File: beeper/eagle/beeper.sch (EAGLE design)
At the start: 32 parts, among them J4 ICSP, T1 MMBT3904, U1 ATA6631, U2 ATMEGA328P, X1 16MHz

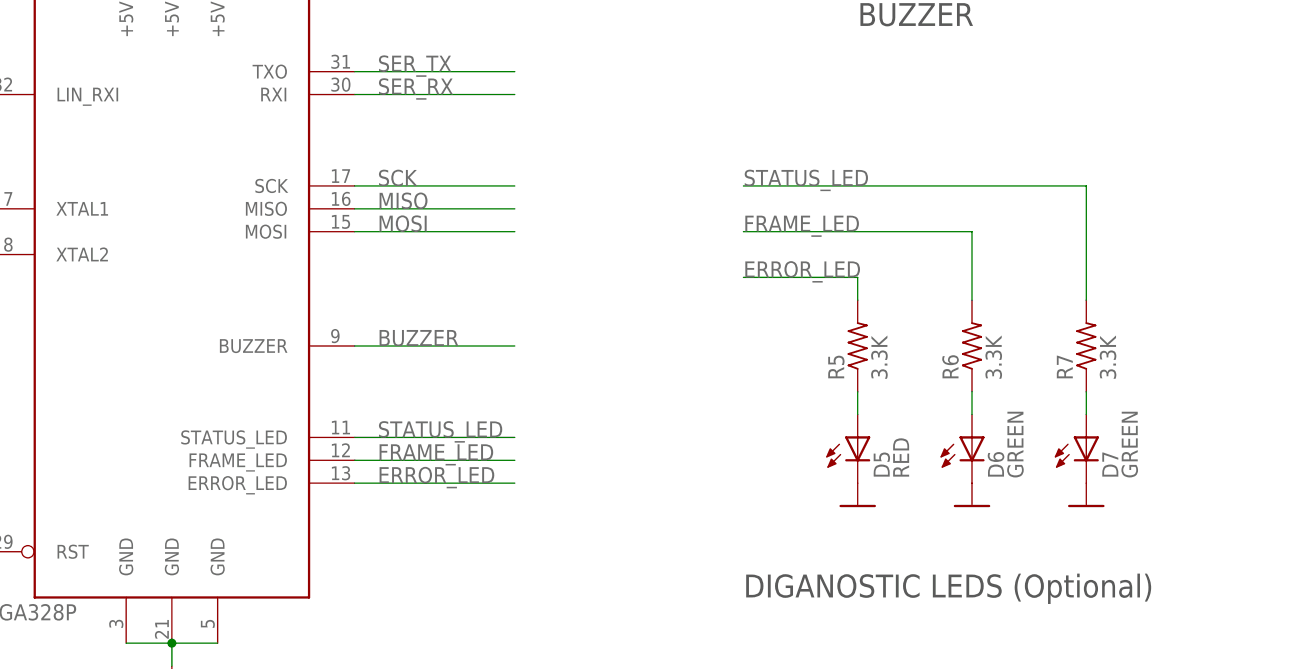
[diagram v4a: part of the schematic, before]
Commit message: Removed the third (status) led.
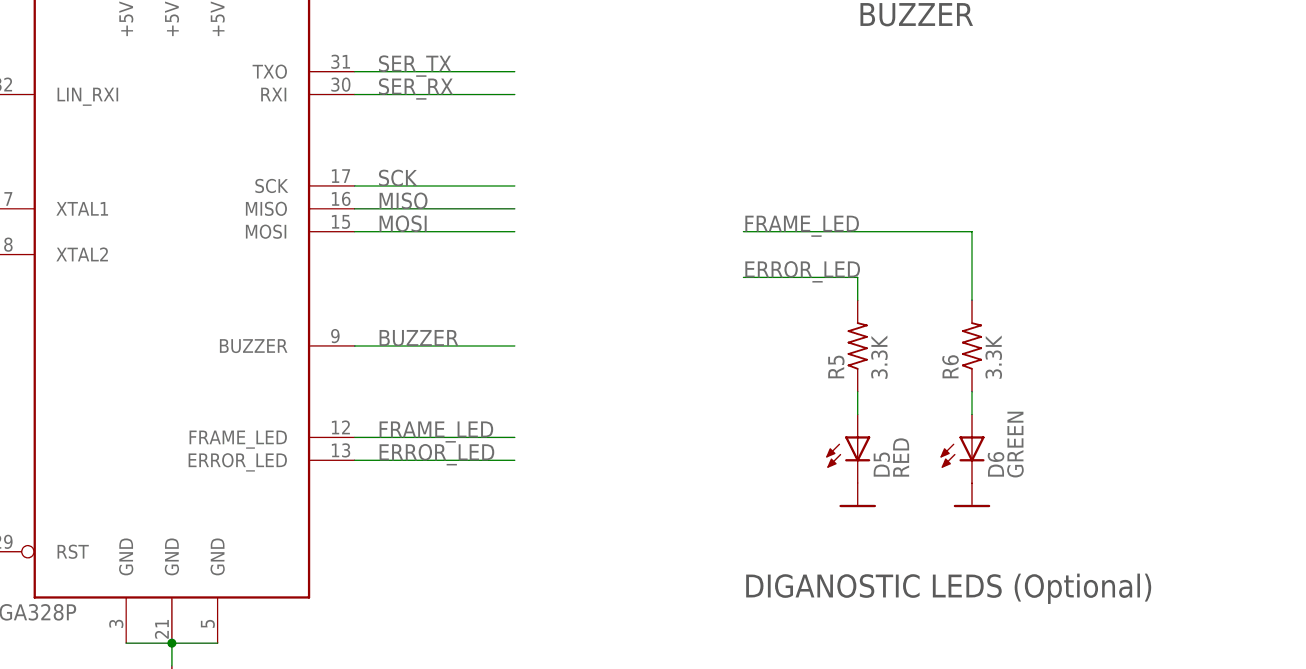
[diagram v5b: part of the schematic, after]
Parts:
- removed D7: GREEN, led:LEDSMT1206
- removed R7: 3.3K, rcl:R-US_R0805
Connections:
- removed net N$2: D7.A, R7.1
- removed net STATUS_LED: R7.2, U2.STATUS_LED
- net GND: no longer D7.C
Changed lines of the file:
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@@
 <part name="R5" library="rcl" deviceset="R-US_" device="R0805" value="3.3K"/>
 <part name="R6" library="rcl" deviceset="R-US_" device="R0805" value="3.3K"/>
-<part name="R7" library="rcl" deviceset="R-US_" device="R0805" value="3.3K"/>
 <part name="C6" library="rcl" deviceset="C-US" device="C0805" value="220pF"/>
 <part name="J1" library="pinhead" deviceset="PINHD-1X3" device=""/>
@@
 <part name="R2" library="rcl" deviceset="R-US_" device="R0805" value="10k"/>
 <part name="GND2" library="beeper" deviceset="GND" device=""/>
-<part name="GND13" library="beeper" deviceset="GND" device=""/>
 <part name="GND16" library="beeper" deviceset="GND" device=""/>
 <part name="J4" library="pinhead" deviceset="PINHD-2X3" device="" value="ICSP"/>
@@
 <part name="D5" library="led" deviceset="LED" device="SMT1206" value="RED"/>
 <part name="D6" library="led" deviceset="LED" device="SMT1206" value="GREEN"/>
-<part name="D7" library="led" deviceset="LED" device="SMT1206" value="GREEN"/>
 <part name="C1" library="rcl" deviceset="CPOL-US" device="UD-6,3X5,8" value="22uF 40V"/>
 <part name="C2" library="rcl" deviceset="C-US" device="C0805" value="0.1uF"/>
@@
 <instance part="R5" gate="G$1" x="261.62" y="99.06" rot="R90"/>
 <instance part="R6" gate="G$1" x="274.32" y="99.06" rot="R90"/>
-<instance part="R7" gate="G$1" x="287.02" y="99.06" rot="R90"/>
 <instance part="C6" gate="G$1" x="99.06" y="154.94"/>
 <instance part="J1" gate="A" x="76.2" y="198.12" rot="MR0"/>
@@
 </instance>
 <instance part="GND2" gate="1" x="274.32" y="81.28"/>
-<instance part="GND13" gate="1" x="287.02" y="81.28"/>
 <instance part="GND16" gate="1" x="185.42" y="60.96"/>
 <instance part="J4" gate="A" x="93.98" y="121.92"/>
@@
 <instance part="D5" gate="G$1" x="261.62" y="88.9"/>
 <instance part="D6" gate="G$1" x="274.32" y="88.9"/>
-<instance part="D7" gate="G$1" x="287.02" y="88.9"/>
 <instance part="C1" gate="G$1" x="152.4" y="195.58" smashed="yes">
 <attribute name="NAME" x="153.416" y="196.215" size="1.778" layer="95"/>
@@
 </segment>
 <segment>
-<pinref part="GND13" gate="1" pin="GND"/>
-<pinref part="D7" gate="G$1" pin="C"/>
-</segment>
-<segment>
 <pinref part="C4" gate="G$1" pin="2"/>
 <pinref part="GND9" gate="1" pin="GND"/>
@@
 <pinref part="C5" gate="G$1" pin="-"/>
 <pinref part="GND10" gate="1" pin="GND"/>
-</segment>
-</net>
-<net name="N$2" class="0">
-<segment>
-<pinref part="R7" gate="G$1" pin="1"/>
-<pinref part="D7" gate="G$1" pin="A"/>
-<wire x1="287.02" y1="93.98" x2="287.02" y2="91.44" width="0.1524" layer="91"/>
 </segment>
 </net>
@@
 </segment>
 <segment>
-<wire x1="205.74" y1="83.82" x2="223.52" y2="83.82" width="0.1524" layer="91"/>
+<wire x1="205.74" y1="86.36" x2="223.52" y2="86.36" width="0.1524" layer="91"/>
 <pinref part="U2" gate="G$1" pin="ERROR_LED"/>
-<label x="208.28" y="83.82" size="1.778" layer="95"/>
+<label x="208.28" y="86.36" size="1.778" layer="95"/>
 </segment>
 </net>
 <net name="FRAME_LED" class="0">
 <segment>
-<wire x1="205.74" y1="86.36" x2="223.52" y2="86.36" width="0.1524" layer="91"/>
+<wire x1="205.74" y1="88.9" x2="223.52" y2="88.9" width="0.1524" layer="91"/>
 <pinref part="U2" gate="G$1" pin="FRAME_LED"/>
-<label x="208.28" y="86.36" size="1.778" layer="95"/>
+<label x="208.28" y="88.9" size="1.778" layer="95"/>
 </segment>
 <segment>
@@
 </segment>
 </net>
-<net name="STATUS_LED" class="0">
-<segment>
-<wire x1="205.74" y1="88.9" x2="223.52" y2="88.9" width="0.1524" layer="91"/>
-<pinref part="U2" gate="G$1" pin="STATUS_LED"/>
-<label x="208.28" y="88.9" size="1.778" layer="95"/>
-</segment>
-<segment>
-<pinref part="R7" gate="G$1" pin="2"/>
-<wire x1="287.02" y1="116.84" x2="287.02" y2="104.14" width="0.1524" layer="91"/>
-<wire x1="248.92" y1="116.84" x2="287.02" y2="116.84" width="0.1524" layer="91"/>
-<label x="248.92" y="116.84" size="1.778" layer="95"/>
-</segment>
-</net>

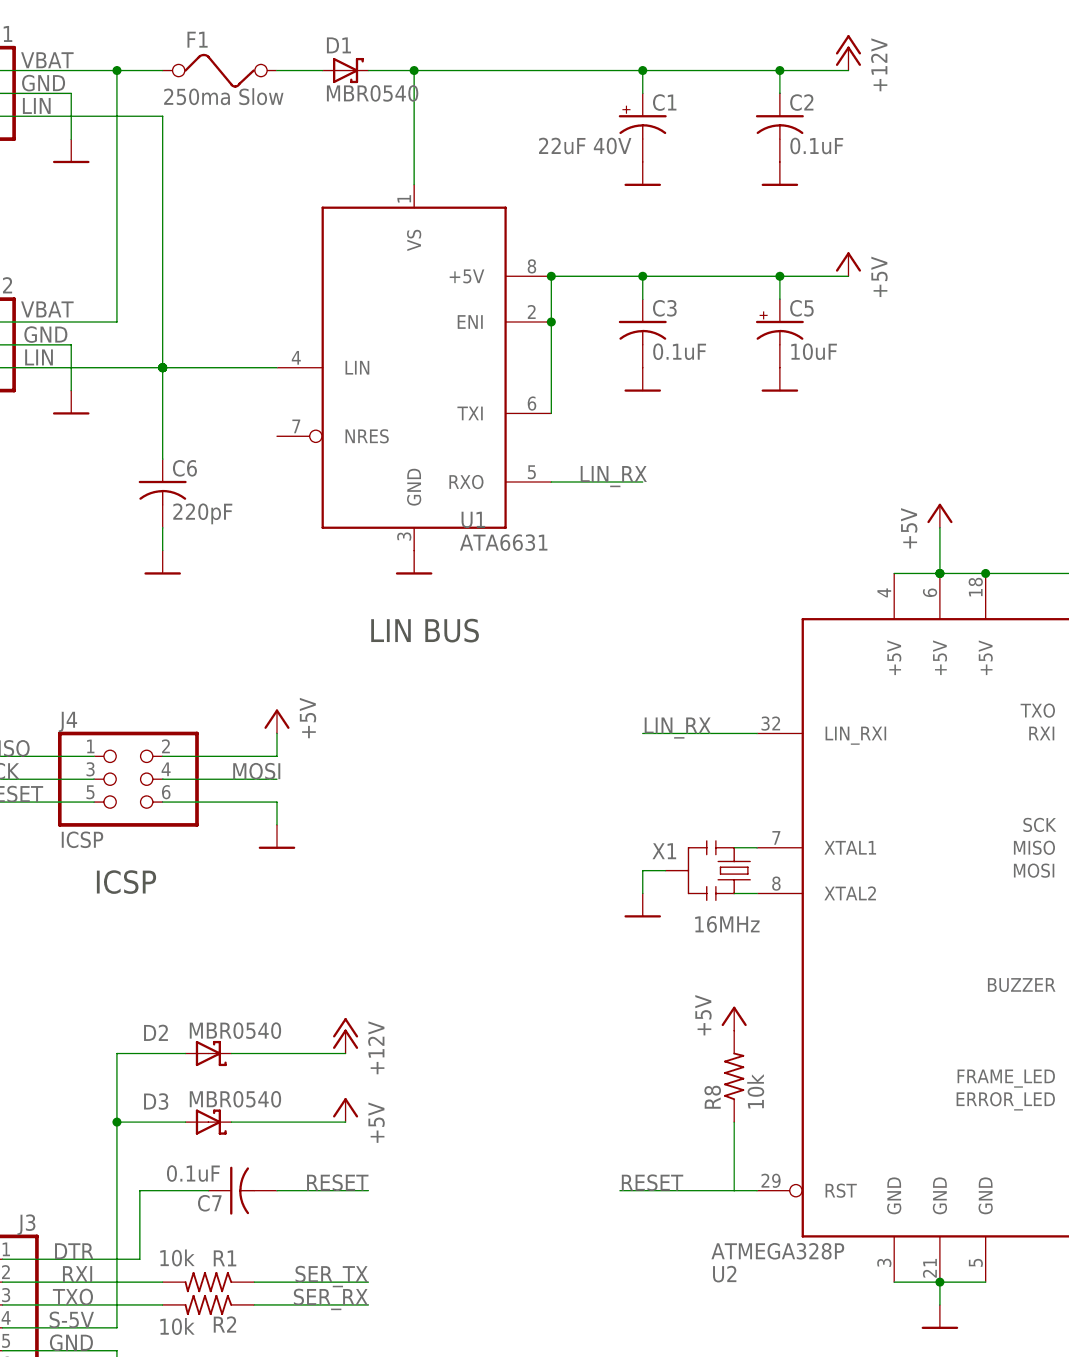
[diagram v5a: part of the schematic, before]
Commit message: Created a clean beeper library. Moved majority of the componnents to the new library.
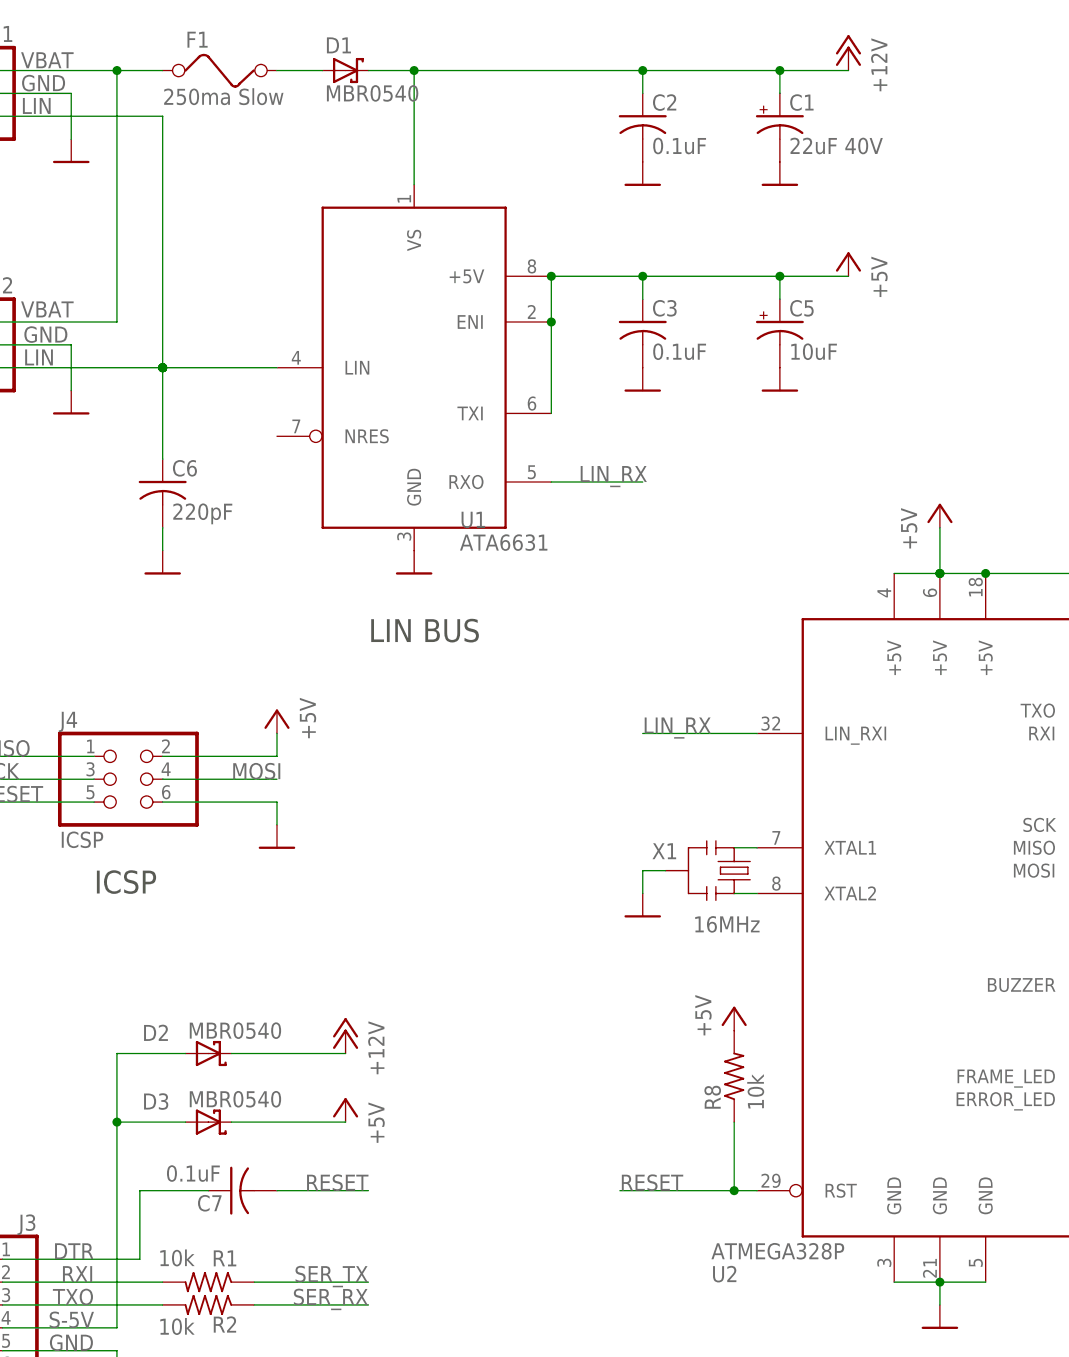
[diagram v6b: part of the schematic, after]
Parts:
- C1: device rcl:CPOL-USUD-6,3X5,8 -> beeper:CPOL-USUD-6,3X5,8
- C2, C3, C6, C7: device rcl:C-USC0805 -> beeper:C-USC0805
- C5: device rcl:CPOL-USA/3216-18R -> beeper:CPOL-USA/3216-18R
- D1, D2, D3, D4: device diode:SMF5.0AT1 -> beeper:SMF5.0AT1
- D5, D6: device led:LEDSMT1206 -> beeper:LEDSMT1206
- J1, J2: device pinhead:PINHD-1X3 -> beeper:PINHD-1X3
- J3: device pinhead:PINHD-1X6 -> beeper:PINHD-1X6
- J4: device pinhead:PINHD-2X3 -> beeper:PINHD-2X3
- R1, R2, R4, R5, R6, R8: device rcl:R-US_R0805 -> beeper:R-US_R0805
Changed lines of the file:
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@@
 </classes>
 <parts>
-<part name="R5" library="rcl" deviceset="R-US_" device="R0805" value="3.3K"/>
-<part name="R6" library="rcl" deviceset="R-US_" device="R0805" value="3.3K"/>
-<part name="C6" library="rcl" deviceset="C-US" device="C0805" value="220pF"/>
-<part name="J1" library="pinhead" deviceset="PINHD-1X3" device=""/>
+<part name="R5" library="beeper" deviceset="R-US_" device="R0805" value="3.3K"/>
+<part name="R6" library="beeper" deviceset="R-US_" device="R0805" value="3.3K"/>
+<part name="C6" library="beeper" deviceset="C-US" device="C0805" value="220pF"/>
+<part name="J1" library="beeper" deviceset="PINHD-1X3" device=""/>
 <part name="FRAME2" library="frames" deviceset="LETTER_L" device=""/>
 <part name="GND3" library="beeper" deviceset="GND" device=""/>
@@
 <part name="GND6" library="beeper" deviceset="GND" device=""/>
 <part name="GND7" library="beeper" deviceset="GND" device=""/>
-<part name="C3" library="rcl" deviceset="C-US" device="C0805" value="0.1uF"/>
+<part name="C3" library="beeper" deviceset="C-US" device="C0805" value="0.1uF"/>
 <part name="GND12" library="beeper" deviceset="GND" device=""/>
-<part name="C7" library="rcl" deviceset="C-US" device="C0805" value="0.1uF"/>
-<part name="P+2" library="supply1" deviceset="+5V" device=""/>
-<part name="R1" library="rcl" deviceset="R-US_" device="R0805" value="10k"/>
-<part name="R2" library="rcl" deviceset="R-US_" device="R0805" value="10k"/>
+<part name="C7" library="beeper" deviceset="C-US" device="C0805" value="0.1uF"/>
+<part name="P+2" library="beeper" deviceset="+5V" device=""/>
+<part name="R1" library="beeper" deviceset="R-US_" device="R0805" value="10k"/>
+<part name="R2" library="beeper" deviceset="R-US_" device="R0805" value="10k"/>
 <part name="GND2" library="beeper" deviceset="GND" device=""/>
 <part name="GND16" library="beeper" deviceset="GND" device=""/>
-<part name="J4" library="pinhead" deviceset="PINHD-2X3" device="" value="ICSP"/>
+<part name="J4" library="beeper" deviceset="PINHD-2X3" device="" value="ICSP"/>
 <part name="GND14" library="beeper" deviceset="GND" device=""/>
-<part name="P+5" library="supply1" deviceset="+5V" device=""/>
+<part name="P+5" library="beeper" deviceset="+5V" device=""/>
 <part name="R3" library="rcl" deviceset="R-US_" device="R0805" value="3.3K"/>
 <part name="T1" library="transistor" deviceset="*-NPN-" device="SOT23-BEC" technology="MMBT3904LT1" value="MMBT3904"/>
 <part name="GND18" library="beeper" deviceset="GND" device=""/>
-<part name="P+3" library="supply1" deviceset="+5V" device=""/>
-<part name="R4" library="rcl" deviceset="R-US_" device="R0805" value="0"/>
-<part name="R8" library="rcl" deviceset="R-US_" device="R0805" value="10k"/>
-<part name="P+6" library="supply1" deviceset="+5V" device=""/>
+<part name="P+3" library="beeper" deviceset="+5V" device=""/>
+<part name="R4" library="beeper" deviceset="R-US_" device="R0805" value="0"/>
+<part name="R8" library="beeper" deviceset="R-US_" device="R0805" value="10k"/>
+<part name="P+6" library="beeper" deviceset="+5V" device=""/>
 <part name="U1" library="beeper" deviceset="ATA6631" device=""/>
-<part name="J3" library="pinhead" deviceset="PINHD-1X6" device=""/>
-<part name="J2" library="pinhead" deviceset="PINHD-1X3" device=""/>
+<part name="J3" library="beeper" deviceset="PINHD-1X6" device=""/>
+<part name="J2" library="beeper" deviceset="PINHD-1X3" device=""/>
 <part name="GND1" library="beeper" deviceset="GND" device=""/>
-<part name="D1" library="diode" deviceset="SMF5.0AT1" device="" value="MBR0540"/>
+<part name="D1" library="beeper" deviceset="SMF5.0AT1" device="" value="MBR0540"/>
 <part name="U2" library="beeper" deviceset="ATMEGA328P" device=""/>
-<part name="D2" library="diode" deviceset="SMF5.0AT1" device="" value="MBR0540"/>
-<part name="D3" library="diode" deviceset="SMF5.0AT1" device="" value="MBR0540"/>
+<part name="D2" library="beeper" deviceset="SMF5.0AT1" device="" value="MBR0540"/>
+<part name="D3" library="beeper" deviceset="SMF5.0AT1" device="" value="MBR0540"/>
 <part name="X1" library="beeper" deviceset="RESONATOR" device="SMD" value="16MHz"/>
 <part name="GND8" library="beeper" deviceset="GND" device=""/>
 <part name="SP1" library="beeper" deviceset="AL60P" device="" value="WT-1205"/>
-<part name="D4" library="diode" deviceset="SMF5.0AT1" device="" value="MBR0540"/>
-<part name="D5" library="led" deviceset="LED" device="SMT1206" value="RED"/>
-<part name="D6" library="led" deviceset="LED" device="SMT1206" value="GREEN"/>
-<part name="C1" library="rcl" deviceset="CPOL-US" device="UD-6,3X5,8" value="22uF 40V"/>
-<part name="C2" library="rcl" deviceset="C-US" device="C0805" value="0.1uF"/>
-<part name="C5" library="rcl" deviceset="CPOL-US" device="A/3216-18R" value="10uF"/>
+<part name="D4" library="beeper" deviceset="SMF5.0AT1" device="" value="MBR0540"/>
+<part name="D5" library="beeper" deviceset="LED" device="SMT1206" value="RED"/>
+<part name="D6" library="beeper" deviceset="LED" device="SMT1206" value="GREEN"/>
+<part name="C1" library="beeper" deviceset="CPOL-US" device="UD-6,3X5,8" value="22uF 40V"/>
+<part name="C2" library="beeper" deviceset="C-US" device="C0805" value="0.1uF"/>
+<part name="C5" library="beeper" deviceset="CPOL-US" device="A/3216-18R" value="10uF"/>
 <part name="C4" library="rcl" deviceset="C-US" device="C0805" value="0.1uF"/>
 <part name="GND9" library="beeper" deviceset="GND" device=""/>
@@
 <part name="GND11" library="beeper" deviceset="GND" device=""/>
 <part name="F1" library="beeper" deviceset="FUSE" device="" value="250ma Slow"/>
-<part name="P+4" library="supply1" deviceset="+5V" device=""/>
-<part name="P+7" library="supply1" deviceset="+12V" device=""/>
-<part name="P+8" library="supply1" deviceset="+5V" device=""/>
-<part name="P+9" library="supply1" deviceset="+12V" device=""/>
+<part name="P+4" library="beeper" deviceset="+5V" device=""/>
+<part name="P+7" library="beeper" deviceset="+12V" device=""/>
+<part name="P+8" library="beeper" deviceset="+5V" device=""/>
+<part name="P+9" library="beeper" deviceset="+12V" device=""/>
 </parts>
 <sheets>
@@
 <instance part="D5" gate="G$1" x="261.62" y="88.9"/>
 <instance part="D6" gate="G$1" x="274.32" y="88.9"/>
-<instance part="C1" gate="G$1" x="152.4" y="195.58" smashed="yes">
-<attribute name="NAME" x="153.416" y="196.215" size="1.778" layer="95"/>
-<attribute name="VALUE" x="140.716" y="191.389" size="1.778" layer="96"/>
-</instance>
-<instance part="C2" gate="G$1" x="167.64" y="195.58"/>
+<instance part="C1" gate="G$1" x="167.64" y="195.58" smashed="yes">
+<attribute name="NAME" x="168.656" y="196.215" size="1.778" layer="95"/>
+<attribute name="VALUE" x="168.656" y="191.389" size="1.778" layer="96"/>
+</instance>
+<instance part="C2" gate="G$1" x="152.4" y="195.58"/>
 <instance part="C5" gate="G$1" x="167.64" y="172.72"/>
 <instance part="C4" gate="G$1" x="205.74" y="144.78" rot="R90"/>
 <instance part="GND9" gate="1" x="215.9" y="139.7"/>
 <instance part="GND10" gate="1" x="167.64" y="165.1"/>
-<instance part="GND15" gate="1" x="152.4" y="187.96"/>
-<instance part="GND17" gate="1" x="167.64" y="187.96"/>
+<instance part="GND15" gate="1" x="167.64" y="187.96"/>
+<instance part="GND17" gate="1" x="152.4" y="187.96"/>
 <instance part="GND11" gate="1" x="127" y="144.78"/>
 <instance part="F1" gate="G$1" x="106.68" y="200.66" smashed="yes">
@@
 <label x="149.86" y="76.2" size="1.778" layer="95"/>
 <wire x1="162.56" y1="76.2" x2="149.86" y2="76.2" width="0.1524" layer="91"/>
+<junction x="162.56" y="76.2"/>
 </segment>
 </net>
@@
 <wire x1="127" y1="200.66" x2="152.4" y2="200.66" width="0.1524" layer="91"/>
 <wire x1="152.4" y1="200.66" x2="167.64" y2="200.66" width="0.1524" layer="91"/>
+<wire x1="167.64" y1="200.66" x2="175.26" y2="200.66" width="0.1524" layer="91"/>
 <wire x1="127" y1="187.96" x2="127" y2="200.66" width="0.1524" layer="91"/>
 <pinref part="U1" gate="G$1" pin="VS"/>
@@
 <junction x="127" y="200.66"/>
 <pinref part="D1" gate="G$1" pin="C"/>
+<pinref part="P+9" gate="1" pin="+12V"/>
+<pinref part="C2" gate="G$1" pin="1"/>
+<wire x1="152.4" y1="198.12" x2="152.4" y2="200.66" width="0.1524" layer="91"/>
 <pinref part="C1" gate="G$1" pin="+"/>
-<wire x1="152.4" y1="198.12" x2="152.4" y2="200.66" width="0.1524" layer="91"/>
-<pinref part="C2" gate="G$1" pin="1"/>
 <wire x1="167.64" y1="198.12" x2="167.64" y2="200.66" width="0.1524" layer="91"/>
 <junction x="152.4" y="200.66"/>
-<pinref part="P+9" gate="1" pin="+12V"/>
-<wire x1="175.26" y1="200.66" x2="167.64" y2="200.66" width="0.1524" layer="91"/>
 <junction x="167.64" y="200.66"/>
 </segment>
